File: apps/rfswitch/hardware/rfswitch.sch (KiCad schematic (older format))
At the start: 51 parts, among them J1 CONN_AC, J10 CONN_O4, J2 CONN_O1, J3 CONN_AC_SW1, J4 CONN_AC_SW2, J5 CONN_01X05, J6 CONN_O2, J7 CONN_AC_SW3, J8 CONN_O3, J9 CONN_AC_SW4, Q1 Q_NPN_BEC, Q2 Q_NPN_BEC, Q3 Q_NPN_BEC, Q4 Q_NPN_BEC, U1 HLK-PM01, U10 G3MB-202P-5V, U2 SFH6916, U3 G3MB-202P-5V, U5 G3MB-202P-5V, U6 TINY328, U8 G3MB-202P-5V

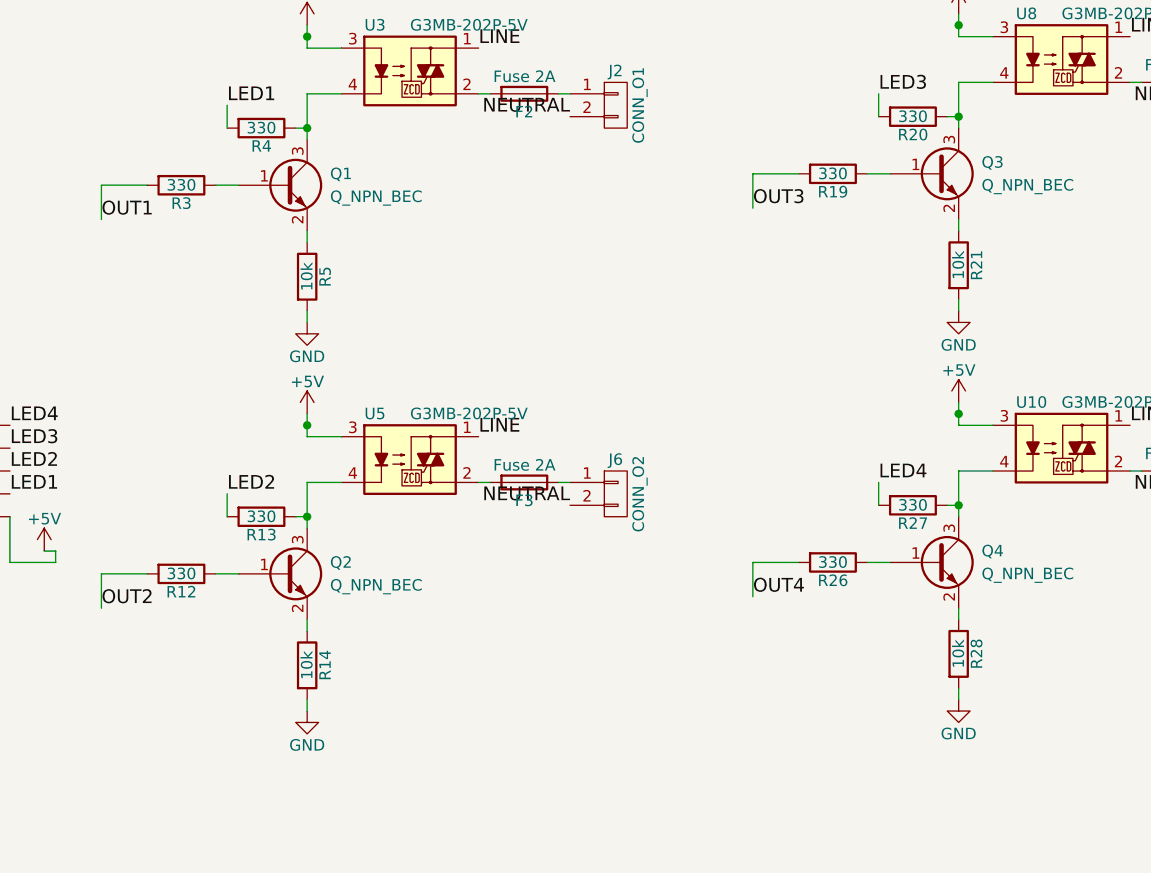
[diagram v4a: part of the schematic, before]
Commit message: Fix pulldown resistor on transistors that wasn't in the right position
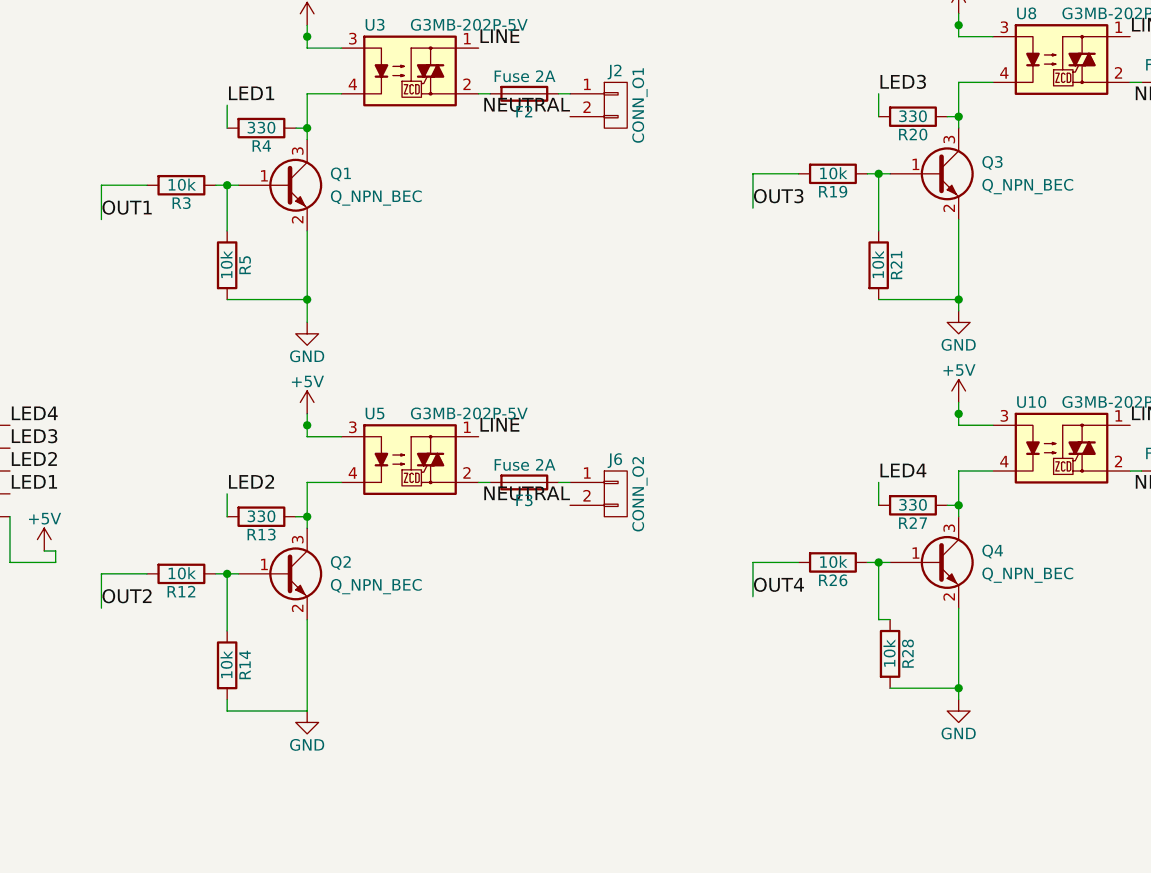
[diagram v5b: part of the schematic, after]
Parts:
- R12, R19, R26, R3: value 330 -> 10k
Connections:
- net GND: now also Q1.2 (E), Q2.2 (E), Q3.2 (E), Q4.2 (E)
- net at Q1.1 (B), R3.1: now also R5.1
- net at Q2.1 (B), R12.1: now also R14.1
- net at Q3.1 (B), R19.1: now also R21.1
- net at Q4.1 (B), R26.1: now also R28.1
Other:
- moved on the sheet: R14, R21, R28, R5
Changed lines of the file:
@@
 P 5850 1700
 F 0 "R3" V 5930 1700 50  0000 C CNN
-F 1 "330" V 5850 1700 50  0000 C CNN
+F 1 "10k" V 5850 1700 50  0000 C CNN
 F 2 "Resistors_SMD:R_0603_HandSoldering" V 5780 1700 50  0001 C CNN
 F 3 "" H 5850 1700 50  0001 C CNN
@@
 L R R5
 U 1 1 594F8F26
-P 6400 2100
-F 0 "R5" V 6480 2100 50  0000 C CNN
-F 1 "10k" V 6400 2100 50  0000 C CNN
-F 2 "Resistors_SMD:R_0603_HandSoldering" V 6330 2100 50  0001 C CNN
-F 3 "" H 6400 2100 50  0001 C CNN
-	1    6400 2100
+P 6050 2050
+F 0 "R5" V 6130 2050 50  0000 C CNN
+F 1 "10k" V 6050 2050 50  0000 C CNN
+F 2 "Resistors_SMD:R_0603_HandSoldering" V 5980 2050 50  0001 C CNN
+F 3 "" H 6050 2050 50  0001 C CNN
+	1    6050 2050
 	1    0    0    -1
 $EndComp
@@
 	1    0    0    -1
 $EndComp
-Wire Wire Line
-	6400 2300 6400 2250
-Wire Wire Line
-	6400 1950 6400 1900
 Wire Wire Line
 	6000 1700 6100 1700
@@
 P 5850 3400
 F 0 "R12" V 5930 3400 50  0000 C CNN
-F 1 "330" V 5850 3400 50  0000 C CNN
+F 1 "10k" V 5850 3400 50  0000 C CNN
 F 2 "Resistors_SMD:R_0603_HandSoldering" V 5780 3400 50  0001 C CNN
 F 3 "" H 5850 3400 50  0001 C CNN
@@
 L R R14
 U 1 1 59614592
-P 6400 3800
-F 0 "R14" V 6480 3800 50  0000 C CNN
-F 1 "10k" V 6400 3800 50  0000 C CNN
-F 2 "Resistors_SMD:R_0603_HandSoldering" V 6330 3800 50  0001 C CNN
-F 3 "" H 6400 3800 50  0001 C CNN
-	1    6400 3800
+P 6050 3800
+F 0 "R14" V 6130 3800 50  0000 C CNN
+F 1 "10k" V 6050 3800 50  0000 C CNN
+F 2 "Resistors_SMD:R_0603_HandSoldering" V 5980 3800 50  0001 C CNN
+F 3 "" H 6050 3800 50  0001 C CNN
+	1    6050 3800
 	1    0    0    -1
 $EndComp
@@
 $EndComp
 Wire Wire Line
-	6400 4000 6400 3950
-Wire Wire Line
-	6400 3650 6400 3600
-Wire Wire Line
 	6000 3400 6100 3400
 Wire Wire Line
@@
 Text Label 7550 3100 2    60   ~ 0
 NEUTRAL
-$Comp
-L Q_NPN_BEC Q2
-U 1 1 596145C8
-P 6300 3400
-F 0 "Q2" H 6500 3450 50  0000 L CNN
-F 1 "Q_NPN_BEC" H 6500 3350 50  0000 L CNN
-F 2 "TO_SOT_Packages_SMD:SOT-23" H 6500 3500 50  0001 C CNN
-F 3 "" H 6300 3400 50  0001 C CNN
-	1    6300 3400
-	1    0    0    -1
-$EndComp
 Text Label 4000 2850 0    60   ~ 0
 OUT1
@@
 P 8700 1650
 F 0 "R19" V 8780 1650 50  0000 C CNN
-F 1 "330" V 8700 1650 50  0000 C CNN
+F 1 "10k" V 8700 1650 50  0000 C CNN
 F 2 "Resistors_SMD:R_0603_HandSoldering" V 8630 1650 50  0001 C CNN
 F 3 "" H 8700 1650 50  0001 C CNN
@@
 L R R21
 U 1 1 596281F7
-P 9250 2050
-F 0 "R21" V 9330 2050 50  0000 C CNN
-F 1 "10k" V 9250 2050 50  0000 C CNN
-F 2 "Resistors_SMD:R_0603_HandSoldering" V 9180 2050 50  0001 C CNN
-F 3 "" H 9250 2050 50  0001 C CNN
-	1    9250 2050
+P 8900 2050
+F 0 "R21" V 8980 2050 50  0000 C CNN
+F 1 "10k" V 8900 2050 50  0000 C CNN
+F 2 "Resistors_SMD:R_0603_HandSoldering" V 8830 2050 50  0001 C CNN
+F 3 "" H 8900 2050 50  0001 C CNN
+	1    8900 2050
 	1    0    0    -1
 $EndComp
@@
 	1    0    0    -1
 $EndComp
-Wire Wire Line
-	9250 2250 9250 2200
-Wire Wire Line
-	9250 1900 9250 1850
 Wire Wire Line
 	8850 1650 8950 1650
@@
 P 8700 3350
 F 0 "R26" V 8780 3350 50  0000 C CNN
-F 1 "330" V 8700 3350 50  0000 C CNN
+F 1 "10k" V 8700 3350 50  0000 C CNN
 F 2 "Resistors_SMD:R_0603_HandSoldering" V 8630 3350 50  0001 C CNN
 F 3 "" H 8700 3350 50  0001 C CNN
@@
 L R R28
 U 1 1 5963C623
-P 9250 3750
-F 0 "R28" V 9330 3750 50  0000 C CNN
-F 1 "10k" V 9250 3750 50  0000 C CNN
-F 2 "Resistors_SMD:R_0603_HandSoldering" V 9180 3750 50  0001 C CNN
-F 3 "" H 9250 3750 50  0001 C CNN
-	1    9250 3750
+P 8950 3750
+F 0 "R28" V 9030 3750 50  0000 C CNN
+F 1 "10k" V 8950 3750 50  0000 C CNN
+F 2 "Resistors_SMD:R_0603_HandSoldering" V 8880 3750 50  0001 C CNN
+F 3 "" H 8950 3750 50  0001 C CNN
+	1    8950 3750
 	1    0    0    -1
 $EndComp
@@
 $EndComp
 Wire Wire Line
-	9250 3950 9250 3900
-Wire Wire Line
-	9250 3600 9250 3550
-Wire Wire Line
 	8850 3350 8950 3350
 Wire Wire Line
@@
 Wire Wire Line
 	3000 5050 2800 5050
+$Comp
+L Q_NPN_BEC Q2
+U 1 1 596145C8
+P 6300 3400
+F 0 "Q2" H 6500 3450 50  0000 L CNN
+F 1 "Q_NPN_BEC" H 6500 3350 50  0000 L CNN
+F 2 "TO_SOT_Packages_SMD:SOT-23" H 6500 3500 50  0001 C CNN
+F 3 "" H 6300 3400 50  0001 C CNN
+	1    6300 3400
+	1    0    0    -1
+$EndComp
+Wire Wire Line
+	6050 3400 6050 3650
+Connection ~ 6050 3400
+Wire Wire Line
+	6050 3950 6050 4000
+Wire Wire Line
+	6050 4000 6400 4000
+Wire Wire Line
+	6400 4000 6400 3600
+Wire Wire Line
+	6050 1900 6050 1700
+Connection ~ 6050 1700
+Wire Wire Line
+	6050 2200 6400 2200
+Wire Wire Line
+	6400 1900 6400 2300
+Connection ~ 6400 2200
+Wire Wire Line
+	8900 1650 8900 1900
+Connection ~ 8900 1650
+Wire Wire Line
+	8900 2200 9250 2200
+Wire Wire Line
+	9250 1850 9250 2250
+Connection ~ 9250 2200
+Wire Wire Line
+	8900 3350 8900 3600
+Wire Wire Line
+	8900 3600 8950 3600
+Connection ~ 8900 3350
+Wire Wire Line
+	8950 3900 9250 3900
+Wire Wire Line
+	9250 3550 9250 3950
+Connection ~ 9250 3900
 $EndSCHEMATC

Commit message: Final board tweaks for construction, and first release of software
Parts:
- added J11: CONN_BTNS, Pin_Headers:Pin_Header_Straight_1x05_Pitch2.54mm, symbol Conn_01x05
- J5: value CONN_01X05 -> CONN_LEDS
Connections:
- net GND: now also J11.1 (Pin_1)
- net SW1: now also J11.2 (Pin_2)
- net SW2: now also J11.3 (Pin_3)
- net SW3: now also J11.4 (Pin_4)
- net SW4: now also J11.5 (Pin_5)
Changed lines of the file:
@@
 $EndComp
 $Comp
-L GND #PWR5
+L GND #PWR01
 U 1 1 594ECD1F
 P 2800 1400
-F 0 "#PWR5" H 2800 1150 50  0001 C CNN
+F 0 "#PWR01" H 2800 1150 50  0001 C CNN
 F 1 "GND" H 2800 1250 50  0000 C CNN
 F 2 "" H 2800 1400 50  0001 C CNN
@@
 	2800 1300 2700 1300
 $Comp
-L +5V #PWR4
+L +5V #PWR02
 U 1 1 594ECD47
 P 2800 1100
-F 0 "#PWR4" H 2800 950 50  0001 C CNN
+F 0 "#PWR02" H 2800 950 50  0001 C CNN
 F 1 "+5V" H 2800 1240 50  0000 C CNN
 F 2 "" H 2800 1100 50  0001 C CNN
@@
 	2800 1200 2700 1200
 $Comp
-L +5V #PWR1
+L +5V #PWR03
 U 1 1 594ECD71
 P 1950 2050
-F 0 "#PWR1" H 1950 1900 50  0001 C CNN
+F 0 "#PWR03" H 1950 1900 50  0001 C CNN
 F 1 "+5V" H 1950 2190 50  0000 C CNN
 F 2 "" H 1950 2050 50  0001 C CNN
@@
 	1950 2050 2200 2050
 $Comp
-L GND #PWR2
+L GND #PWR04
 U 1 1 594ECD9D
 P 1950 2300
-F 0 "#PWR2" H 1950 2050 50  0001 C CNN
+F 0 "#PWR04" H 1950 2050 50  0001 C CNN
 F 1 "GND" H 1950 2150 50  0000 C CNN
 F 2 "" H 1950 2300 50  0001 C CNN
@@
 	2150 3950 2200 3950
 $Comp
-L +3.3V #PWR3
+L +3.3V #PWR05
 U 1 1 594EDF33
 P 2050 1850
-F 0 "#PWR3" H 2050 1700 50  0001 C CNN
+F 0 "#PWR05" H 2050 1700 50  0001 C CNN
 F 1 "+3.3V" H 2050 1990 50  0000 C CNN
 F 2 "" H 2050 1850 50  0001 C CNN
@@
 	2050 1950 2050 1850
 $Comp
-L +3.3V #PWR6
+L +3.3V #PWR06
 U 1 1 594EDF92
 P 3000 3550
-F 0 "#PWR6" H 3000 3400 50  0001 C CNN
+F 0 "#PWR06" H 3000 3400 50  0001 C CNN
 F 1 "+3.3V" H 3000 3690 50  0000 C CNN
 F 2 "" H 3000 3550 50  0001 C CNN
@@
 	3000 3550 3000 3650
 $Comp
-L GND #PWR7
+L GND #PWR07
 U 1 1 594EDFF3
 P 3000 4050
-F 0 "#PWR7" H 3000 3800 50  0001 C CNN
+F 0 "#PWR07" H 3000 3800 50  0001 C CNN
 F 1 "GND" H 3000 3900 50  0000 C CNN
 F 2 "" H 3000 4050 50  0001 C CNN
@@
 $EndComp
 $Comp
-L GND #PWR16
+L GND #PWR08
 U 1 1 594F9167
 P 6400 2300
-F 0 "#PWR16" H 6400 2050 50  0001 C CNN
+F 0 "#PWR08" H 6400 2050 50  0001 C CNN
 F 1 "GND" H 6400 2150 50  0000 C CNN
 F 2 "" H 6400 2300 50  0001 C CNN
@@
 	6400 1300 6550 1300
 $Comp
-L +5V #PWR15
+L +5V #PWR09
 U 1 1 594F9818
 P 6400 1000
-F 0 "#PWR15" H 6400 850 50  0001 C CNN
+F 0 "#PWR09" H 6400 850 50  0001 C CNN
 F 1 "+5V" H 6400 1140 50  0000 C CNN
 F 2 "" H 6400 1000 50  0001 C CNN
@@
 $EndComp
 $Comp
-L +3.3V #PWR11
+L +3.3V #PWR010
 U 1 1 59614347
 P 3500 4200
-F 0 "#PWR11" H 3500 4050 50  0001 C CNN
+F 0 "#PWR010" H 3500 4050 50  0001 C CNN
 F 1 "+3.3V" H 3500 4340 50  0000 C CNN
 F 2 "" H 3500 4200 50  0001 C CNN
@@
 $EndComp
 $Comp
-L GND #PWR8
+L GND #PWR011
 U 1 1 5961434F
 P 3000 4300
-F 0 "#PWR8" H 3000 4050 50  0001 C CNN
+F 0 "#PWR011" H 3000 4050 50  0001 C CNN
 F 1 "GND" H 3000 4150 50  0000 C CNN
 F 2 "" H 3000 4300 50  0001 C CNN
@@
 $EndComp
 $Comp
-L GND #PWR18
+L GND #PWR012
 U 1 1 59614598
 P 6400 4000
-F 0 "#PWR18" H 6400 3750 50  0001 C CNN
+F 0 "#PWR012" H 6400 3750 50  0001 C CNN
 F 1 "GND" H 6400 3850 50  0000 C CNN
 F 2 "" H 6400 4000 50  0001 C CNN
@@
 	6400 3000 6550 3000
 $Comp
-L +5V #PWR17
+L +5V #PWR013
 U 1 1 596145A3
 P 6400 2700
-F 0 "#PWR17" H 6400 2550 50  0001 C CNN
+F 0 "#PWR013" H 6400 2550 50  0001 C CNN
 F 1 "+5V" H 6400 2840 50  0000 C CNN
 F 2 "" H 6400 2700 50  0001 C CNN
@@
 P 4900 2950
 F 0 "J5" H 4900 3250 50  0000 C CNN
-F 1 "CONN_01X05" V 5000 2950 50  0000 C CNN
+F 1 "CONN_LEDS" V 5000 2950 50  0000 C CNN
 F 2 "Pin_Headers:Pin_Header_Straight_1x05_Pitch2.54mm" H 4900 2950 50  0001 C CNN
 F 3 "" H 4900 2950 50  0001 C CNN
@@
 $EndComp
 $Comp
-L +5V #PWR14
+L +5V #PWR014
 U 1 1 5961493D
 P 5250 3300
-F 0 "#PWR14" H 5250 3150 50  0001 C CNN
+F 0 "#PWR014" H 5250 3150 50  0001 C CNN
 F 1 "+5V" H 5250 3440 50  0000 C CNN
 F 2 "" H 5250 3300 50  0001 C CNN
@@
 $EndComp
 $Comp
-L +3.3V #PWR12
+L +3.3V #PWR015
 U 1 1 596273E2
 P 3500 4500
-F 0 "#PWR12" H 3500 4350 50  0001 C CNN
+F 0 "#PWR015" H 3500 4350 50  0001 C CNN
 F 1 "+3.3V" H 3500 4640 50  0000 C CNN
 F 2 "" H 3500 4500 50  0001 C CNN
@@
 $EndComp
 $Comp
-L GND #PWR9
+L GND #PWR016
 U 1 1 596273EA
 P 3000 4600
-F 0 "#PWR9" H 3000 4350 50  0001 C CNN
+F 0 "#PWR016" H 3000 4350 50  0001 C CNN
 F 1 "GND" H 3000 4450 50  0000 C CNN
 F 2 "" H 3000 4600 50  0001 C CNN
@@
 $EndComp
 $Comp
-L GND #PWR20
+L GND #PWR017
 U 1 1 596281FD
 P 9250 2250
-F 0 "#PWR20" H 9250 2000 50  0001 C CNN
+F 0 "#PWR017" H 9250 2000 50  0001 C CNN
 F 1 "GND" H 9250 2100 50  0000 C CNN
 F 2 "" H 9250 2250 50  0001 C CNN
@@
 	9250 1250 9400 1250
 $Comp
-L +5V #PWR19
+L +5V #PWR018
 U 1 1 59628208
 P 9250 950
-F 0 "#PWR19" H 9250 800 50  0001 C CNN
+F 0 "#PWR018" H 9250 800 50  0001 C CNN
 F 1 "+5V" H 9250 1090 50  0000 C CNN
 F 2 "" H 9250 950 50  0001 C CNN
@@
 $EndComp
 $Comp
-L +3.3V #PWR13
+L +3.3V #PWR019
 U 1 1 5963BDD0
 P 3500 4800
-F 0 "#PWR13" H 3500 4650 50  0001 C CNN
+F 0 "#PWR019" H 3500 4650 50  0001 C CNN
 F 1 "+3.3V" H 3500 4940 50  0000 C CNN
 F 2 "" H 3500 4800 50  0001 C CNN
@@
 $EndComp
 $Comp
-L GND #PWR10
+L GND #PWR020
 U 1 1 5963BDD8
 P 3000 5050
-F 0 "#PWR10" H 3000 4800 50  0001 C CNN
+F 0 "#PWR020" H 3000 4800 50  0001 C CNN
 F 1 "GND" H 3000 4900 50  0000 C CNN
 F 2 "" H 3000 5050 50  0001 C CNN
@@
 $EndComp
 $Comp
-L GND #PWR22
+L GND #PWR021
 U 1 1 5963C629
 P 9250 3950
-F 0 "#PWR22" H 9250 3700 50  0001 C CNN
+F 0 "#PWR021" H 9250 3700 50  0001 C CNN
 F 1 "GND" H 9250 3800 50  0000 C CNN
 F 2 "" H 9250 3950 50  0001 C CNN
@@
 	9250 2950 9400 2950
 $Comp
-L +5V #PWR21
+L +5V #PWR022
 U 1 1 5963C634
 P 9250 2650
-F 0 "#PWR21" H 9250 2500 50  0001 C CNN
+F 0 "#PWR022" H 9250 2500 50  0001 C CNN
 F 1 "+5V" H 9250 2790 50  0000 C CNN
 F 2 "" H 9250 2650 50  0001 C CNN
@@
 	9250 3550 9250 3950
 Connection ~ 9250 3900
+$Comp
+L Conn_01x05 J11
+U 1 1 5A231209
+P 4900 2250
+F 0 "J11" H 4900 2550 50  0000 C CNN
+F 1 "CONN_BTNS" H 4900 1950 50  0000 C CNN
+F 2 "Pin_Headers:Pin_Header_Straight_1x05_Pitch2.54mm" H 4900 2250 50  0001 C CNN
+F 3 "" H 4900 2250 50  0001 C CNN
+	1    4900 2250
+	-1   0    0    1
+$EndComp
+$Comp
+L GND #PWR023
+U 1 1 5A231700
+P 5200 2450
+F 0 "#PWR023" H 5200 2200 50  0001 C CNN
+F 1 "GND" H 5200 2300 50  0000 C CNN
+F 2 "" H 5200 2450 50  0001 C CNN
+F 3 "" H 5200 2450 50  0001 C CNN
+	1    5200 2450
+	1    0    0    -1
+$EndComp
+Wire Wire Line
+	5200 2450 5100 2450
+Text Label 5100 2350 0    60   ~ 0
+SW1
+Text Label 5100 2250 0    60   ~ 0
+SW2
+Text Label 5100 2150 0    60   ~ 0
+SW3
+Text Label 5100 2050 0    60   ~ 0
+SW4
 $EndSCHEMATC
